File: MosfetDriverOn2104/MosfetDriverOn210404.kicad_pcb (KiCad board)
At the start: 2 copper layers, 99.8 x 100.6 mm, 88 parts, among them J1 I2C HDR, J10 ENCODER HDR, J11 CROSS CONN, J12 motor, J2 AVR-ISP-6, J3 I2C HDR, J4 Screw_Terminal_01x02, J5 I2C HDR, J6 UART HDR, J7 5V HDR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

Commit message: necktie pattern
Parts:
- C12, CB3, CB6, D2, D8, R3, U2: moved to B.Cu
- R22, R23, R24, R25, R26, R4: moved to F.Cu
- moved C9 140.9 mm to (148.6, 96.0), turned to 90 degrees
- moved Q4 137.5 mm to (157.3, 75.2), turned to 45 degrees
- moved C1 134.8 mm to (126.7, 94.2), turned to 315 degrees
- moved D7 133.1 mm to (151.5, 81.3), turned to 45 degrees
- moved R15 131.2 mm to (153.6, 83.2), turned to 225 degrees
- moved Q3 131.0 mm to (142.8, 88.6), turned to 45 degrees
- moved CB6 128.4 mm to (156.0, 96.2), turned to 90 degrees
- moved CB3 126.6 mm to (158.1, 94.9)
- moved U5 126.4 mm to (160.9, 98.9), turned to 180 degrees
- moved D6 126.1 mm to (139.1, 95.5), turned to 135 degrees
- moved D8 124.5 mm to (156.9, 102.5), turned to 0 degrees
- moved R14 122.0 mm to (143.0, 93.7), turned to 225 degrees
- moved D5 119.3 mm to (184.2, 92.0), turned to 315 degrees
- moved R6 119.2 mm to (179.9, 93.1), turned to 45 degrees
- moved R5 113.3 mm to (169.8, 106.7), turned to 45 degrees
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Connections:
- J1 pad 1: GND -> /SCL
- J1 pad 2: /SCL -> /SDA
- J1 pad 3: /SDA -> GND
- J10 pad 2: /B -> +5V
- J10 pad 3: /A -> /B
- J10 pad 4: +5V -> /A
- J3 pad 1: GND -> /SCL
- J3 pad 2: /SCL -> /SDA
- J3 pad 3: /SDA -> GND
- J5 pad 1: GND -> /SCL
- J5 pad 2: /SCL -> /SDA
- J5 pad 3: /SDA -> GND
- J6 pad 2: /TX -> +5V
- J6 pad 3: /RX -> Net-(J6-Pad3)
- J6 pad 4: +5V -> Net-(J6-Pad4)
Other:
- board size 99.8 x 100.6 mm -> 99.8 x 108.6 mm

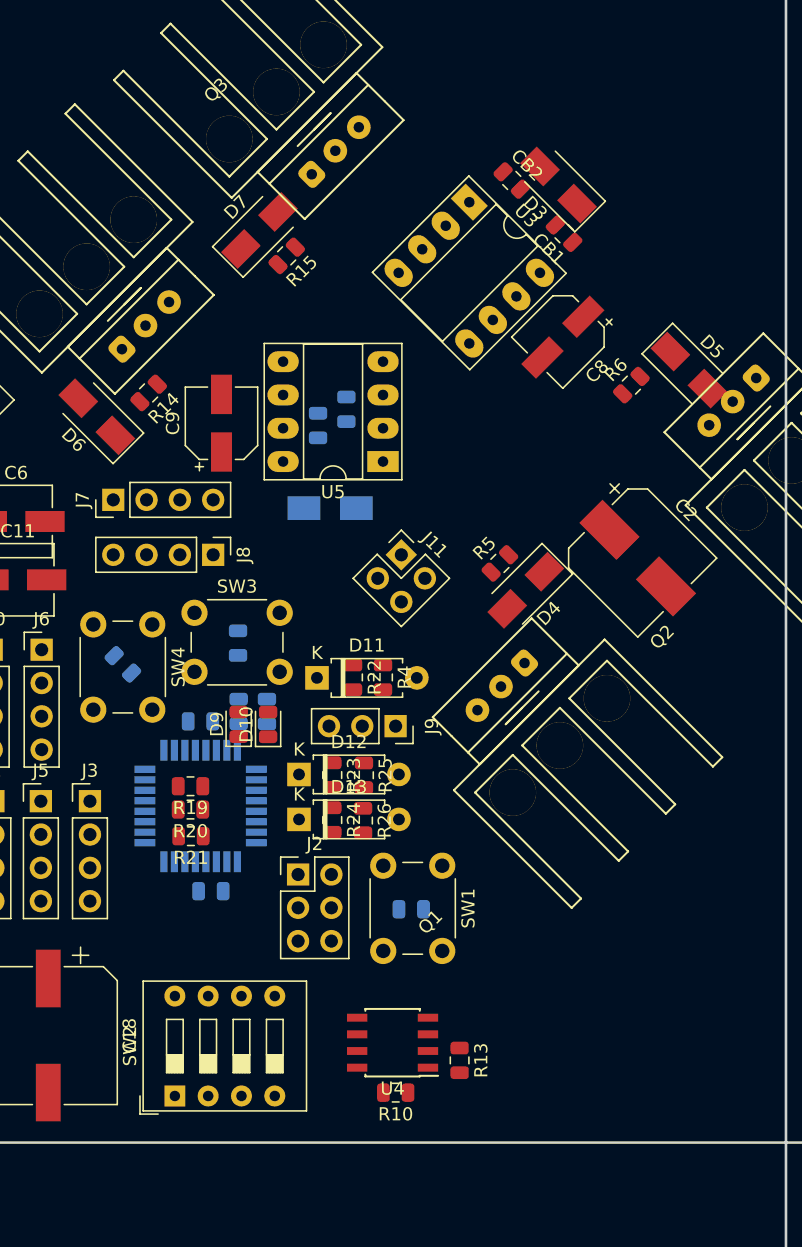
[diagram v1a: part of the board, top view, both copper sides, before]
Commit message: add model for mosfet
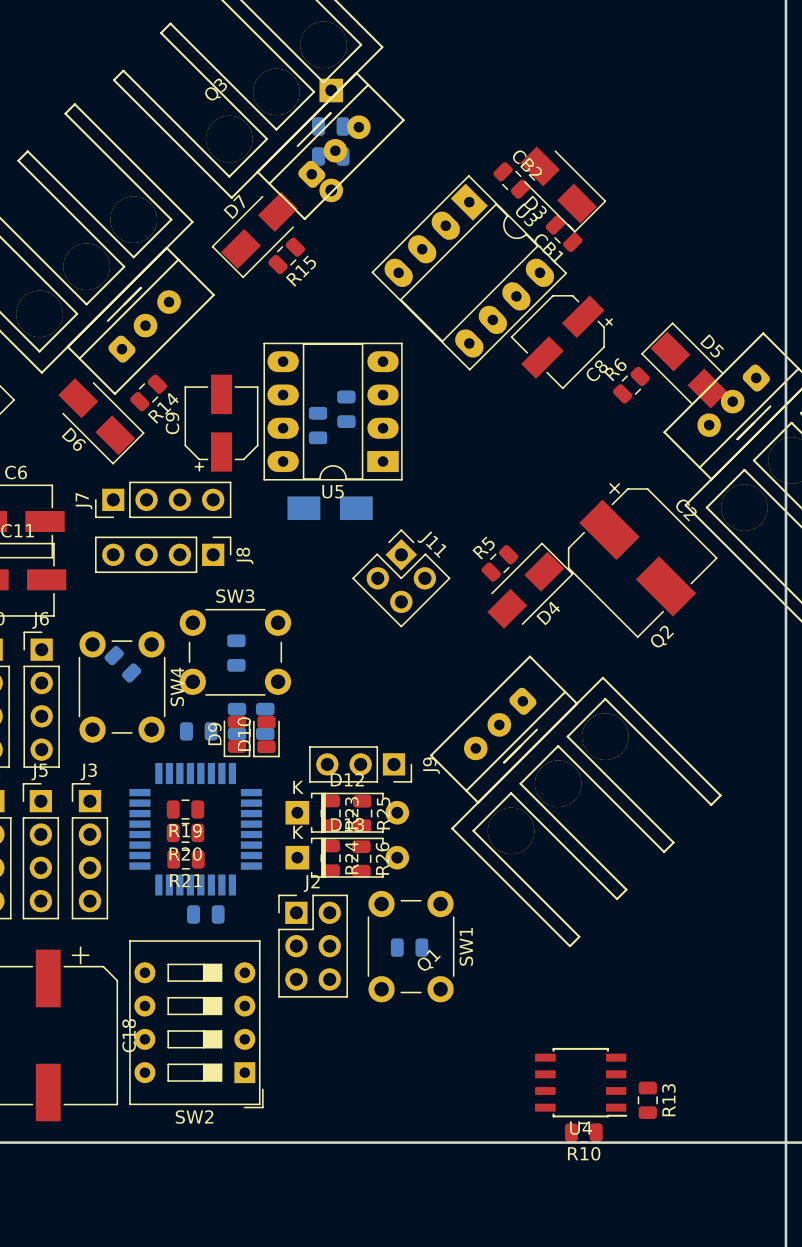
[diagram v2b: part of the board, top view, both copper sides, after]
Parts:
- D11, R22, R4: moved to B.Cu
- moved D11 44.8 mm to (157.0, 70.6), turned to 270 degrees
- moved R22 42.0 mm to (156.9, 73.4), turned to 0 degrees
- moved R4 39.9 mm to (156.9, 75.7), turned to 0 degrees
- moved R10 14.7 mm to (176.2, 150.1)
- moved R13 14.7 mm to (181.1, 147.7)
- moved U4 14.7 mm to (176.0, 146.3)
- moved SW2 5.62 mm to (150.4, 145.5), turned to 180 degrees
- moved R26 2.92 mm to (159.3, 129.2)
- moved D12 2.92 mm to (154.4, 125.7)
- moved R25 2.92 mm to (159.3, 125.8)
- moved J9 2.92 mm to (161.7, 122.0)
- moved R23 2.92 mm to (156.9, 125.8)
- moved R24 2.92 mm to (156.9, 129.2)
- moved C10 2.92 mm to (162.9, 136.0)
- moved D13 2.92 mm to (154.4, 129.1)
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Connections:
- SW2 pad 5: +5V -> GND
- SW2 pad 6: +5V -> GND
- SW2 pad 7: +5V -> GND
- SW2 pad 8: +5V -> GND

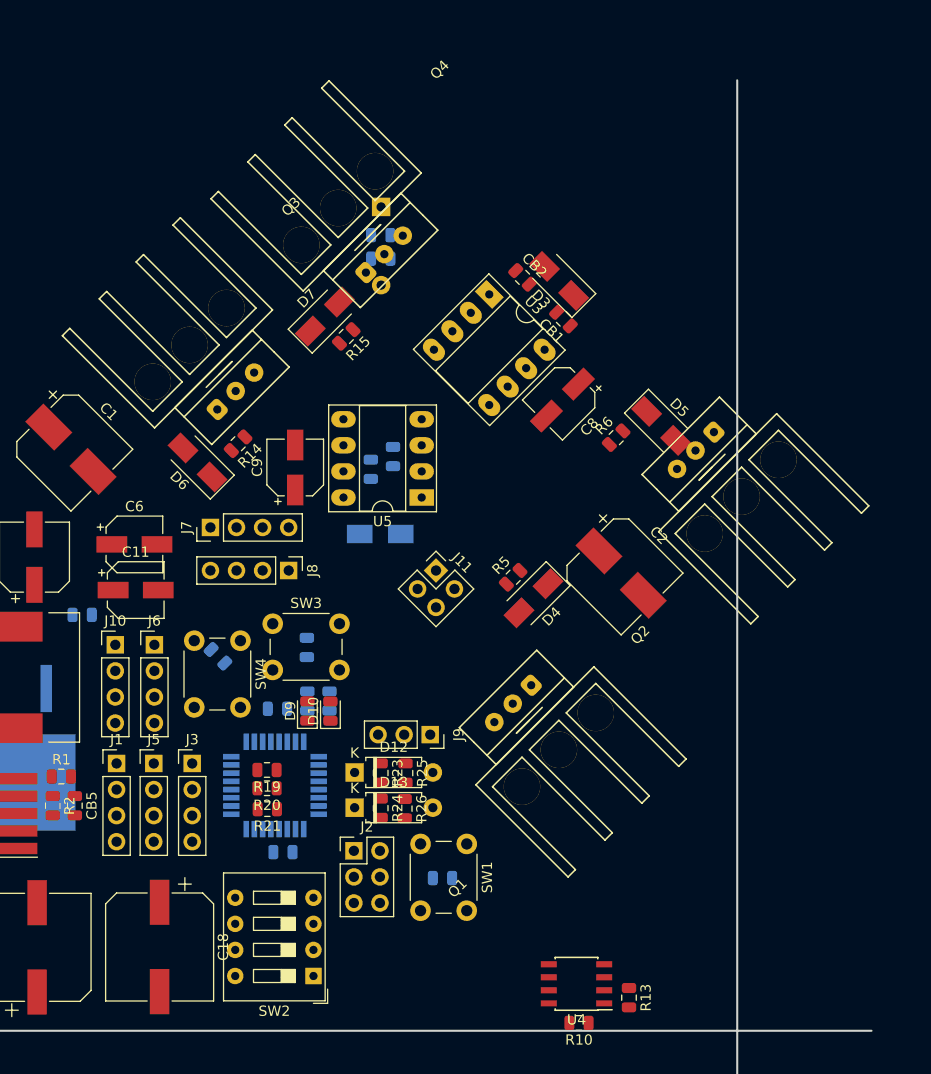
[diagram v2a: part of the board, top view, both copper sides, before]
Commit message: MOdified Footprint for TO220,REF https://github.com/botwot/kicad-lib/
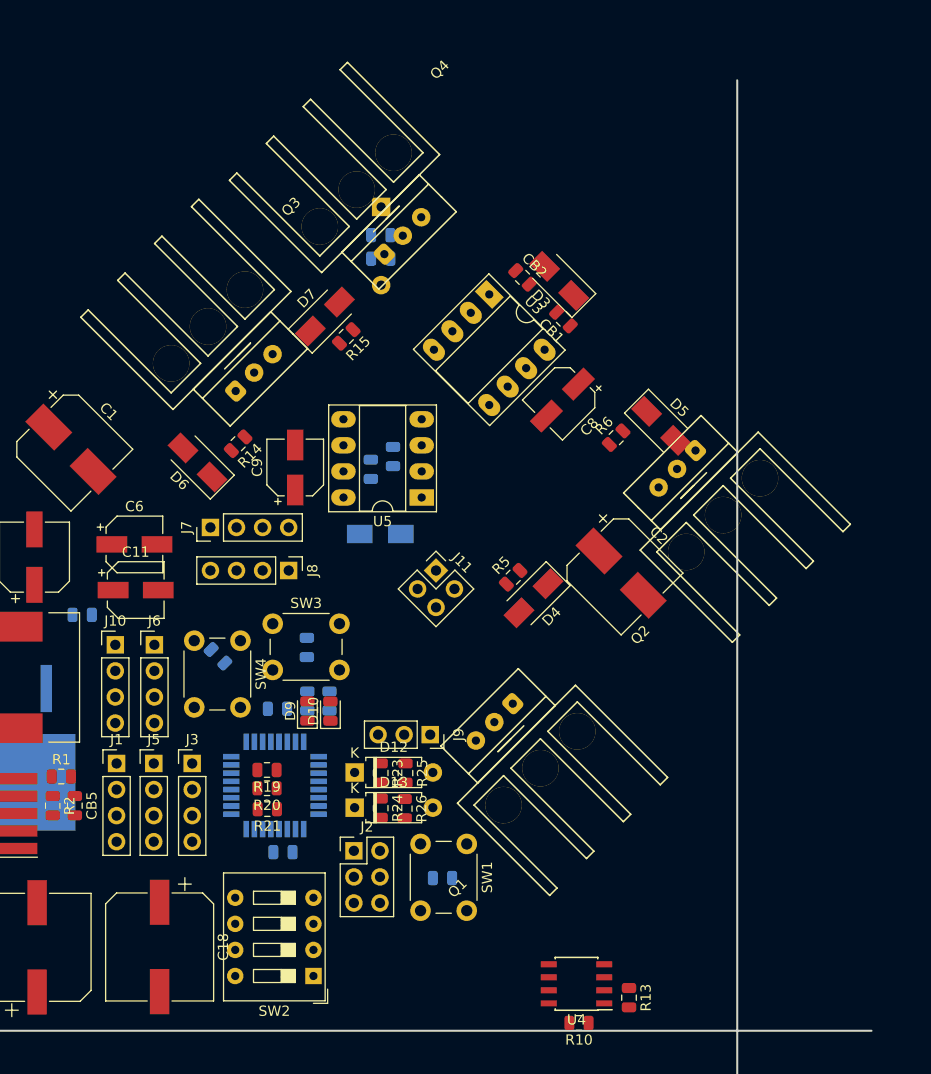
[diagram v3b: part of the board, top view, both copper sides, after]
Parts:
- Q1, Q2, Q3, Q4: footprint Footprints:TO220_HS_SCREW -> TO220_HS_SCREW:TO220_HS_SCREW

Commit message: placement almost finalized !
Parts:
- CB3, CB6, D2, D8, R3: moved to F.Cu
- R11, R12, R7, R8, R9: moved to B.Cu
- moved J12 164.4 mm to (171.4, 75.5), turned to 310 degrees
- moved R11 137.5 mm to (192.1, 63.0), turned to 210 degrees
- moved R12 135.3 mm to (193.1, 64.9), turned to 210 degrees
- moved R9 133.0 mm to (194.4, 67.0), turned to 210 degrees
- moved R7 130.9 mm to (195.4, 69.0), turned to 210 degrees
- moved R8 129.1 mm to (196.5, 70.8), turned to 210 degrees
- moved R3 55.1 mm to (151.3, 107.7)
- moved D2 51.7 mm to (151.3, 104.8), turned to 180 degrees
- moved D11 50.5 mm to (156.1, 121.1), turned to 90 degrees
- moved R22 45.0 mm to (156.1, 118.4), turned to 180 degrees
- moved R4 40.4 mm to (156.1, 116.1), turned to 180 degrees
- moved C2 30.2 mm to (165.0, 132.4), turned to 220 degrees
- moved CB2 14.9 mm to (160.9, 88.6), turned to 180 degrees
- moved D8 14.2 mm to (154.5, 88.5)
- moved CB6 14.1 mm to (142.2, 98.9), turned to 140 degrees
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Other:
- board size 99.8 x 108.6 mm -> 93.5 x 94.9 mm

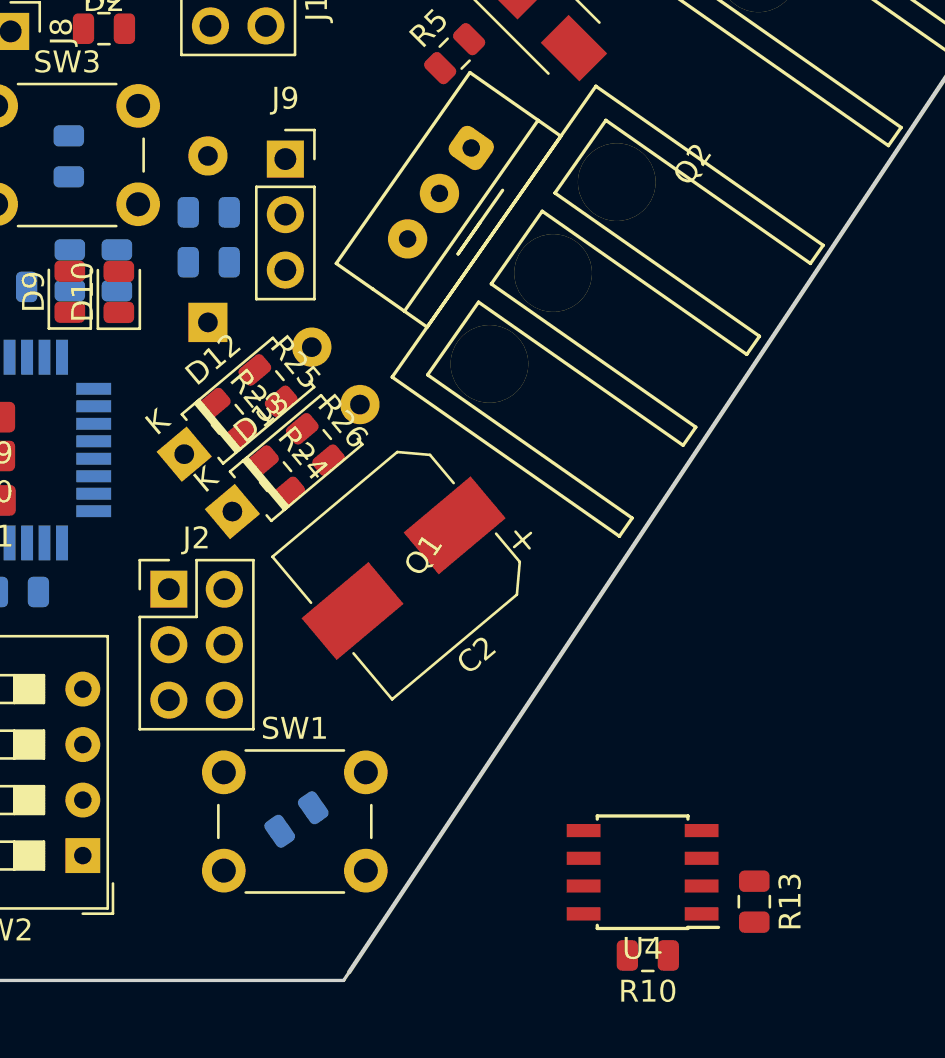
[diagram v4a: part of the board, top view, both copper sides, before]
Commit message: 358 placed
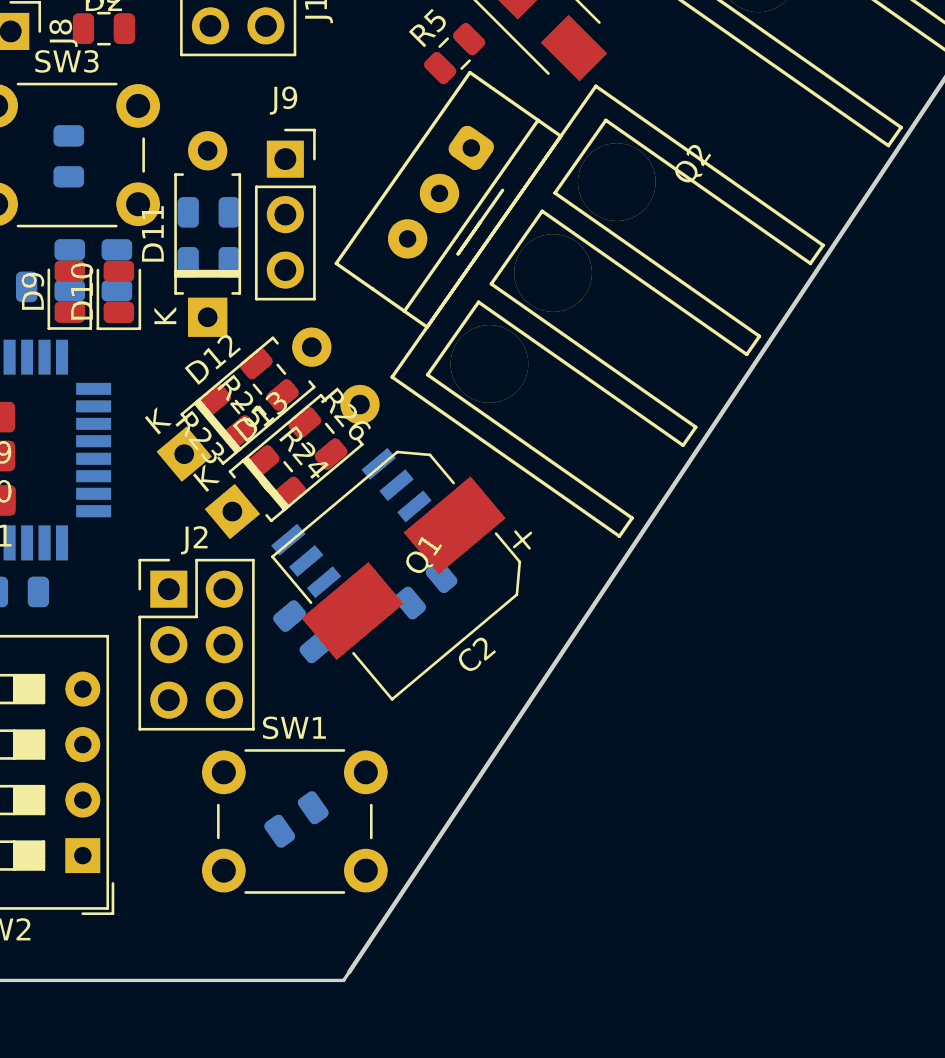
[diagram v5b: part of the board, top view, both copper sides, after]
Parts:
- D11: moved to F.Cu
- R10, R13, U4: moved to B.Cu
- moved R13 24.1 mm to (160.4, 135.3), turned to 310 degrees
- moved U4 20.2 mm to (163.1, 130.8), turned to 40 degrees
- moved R10 19.6 mm to (166.1, 133.4), turned to 40 degrees
- moved R26 0.30 mm to (161.1, 126.4)
- moved R25 0.30 mm to (158.9, 123.7), turned to 130 degrees
- moved D11 0.24 mm to (156.1, 120.9)
- moved R23 0.18 mm to (157.0, 125.4), turned to 130 degrees

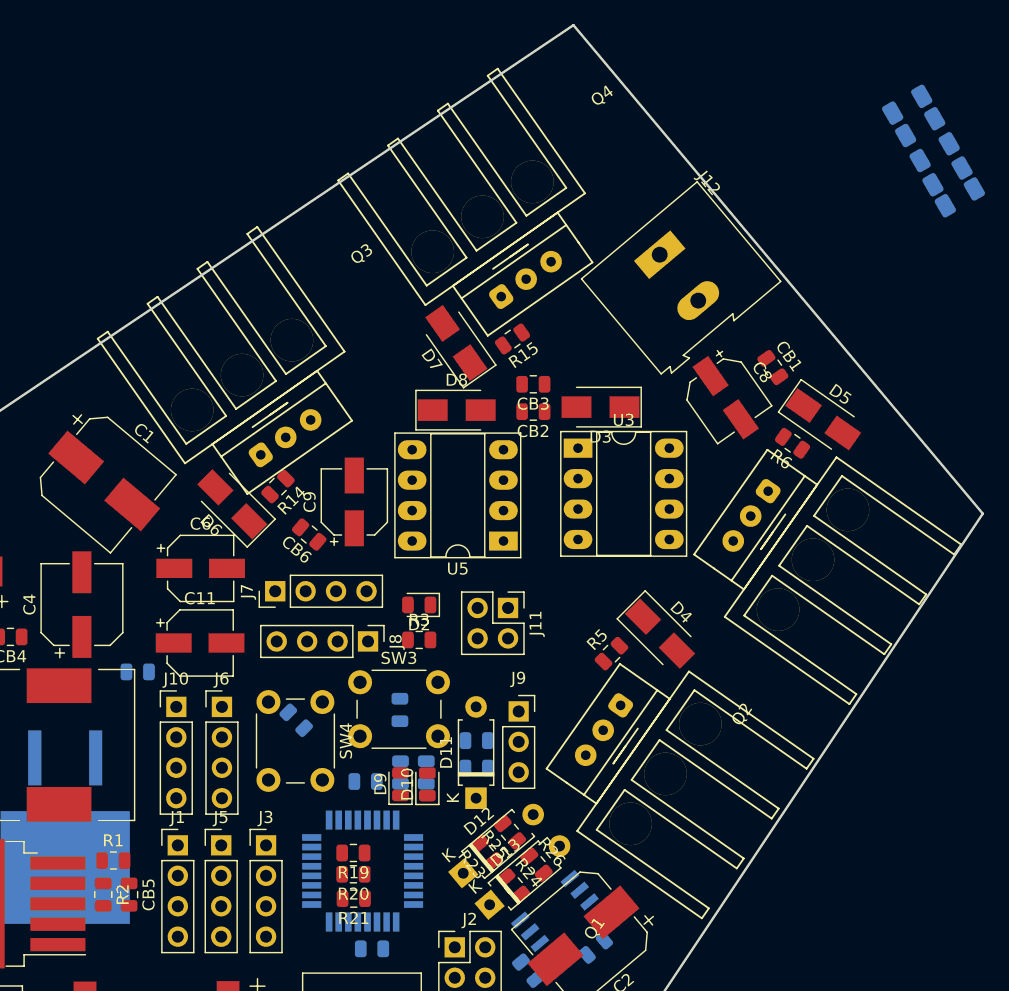
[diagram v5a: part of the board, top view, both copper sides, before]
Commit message: resistor footprint changed
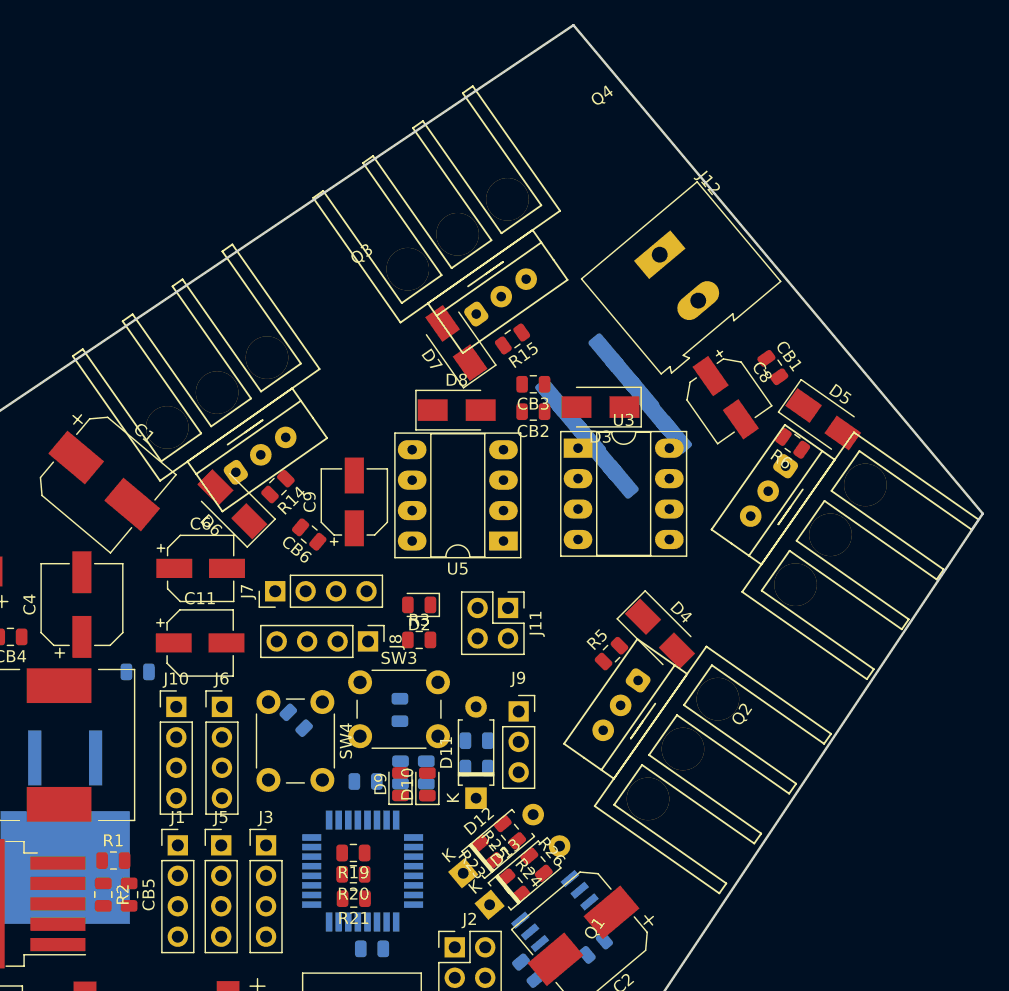
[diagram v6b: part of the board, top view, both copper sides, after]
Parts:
- Q1, Q2, Q3, Q4: footprint TO220_HS_SCREW:TO220_HS_SCREW -> Footprints:TO220_HS_SCREW
- R11, R12, R7, R8, R9: footprint Resistor_SMD:R_1206_3216Metric -> Resistor_SMD:R_2512_6332Metric
- moved R11 35.4 mm to (164.7, 85.6), turned to 220 degrees
- moved R12 35.1 mm to (166.1, 87.2), turned to 220 degrees
- moved R9 34.7 mm to (167.7, 89.1), turned to 220 degrees
- moved R7 34.3 mm to (169.1, 90.9), turned to 220 degrees
- moved R8 33.9 mm to (170.4, 92.4), turned to 220 degrees
